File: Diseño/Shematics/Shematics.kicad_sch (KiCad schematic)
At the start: 2 parts, among them U1 ESP32-WROOM-E

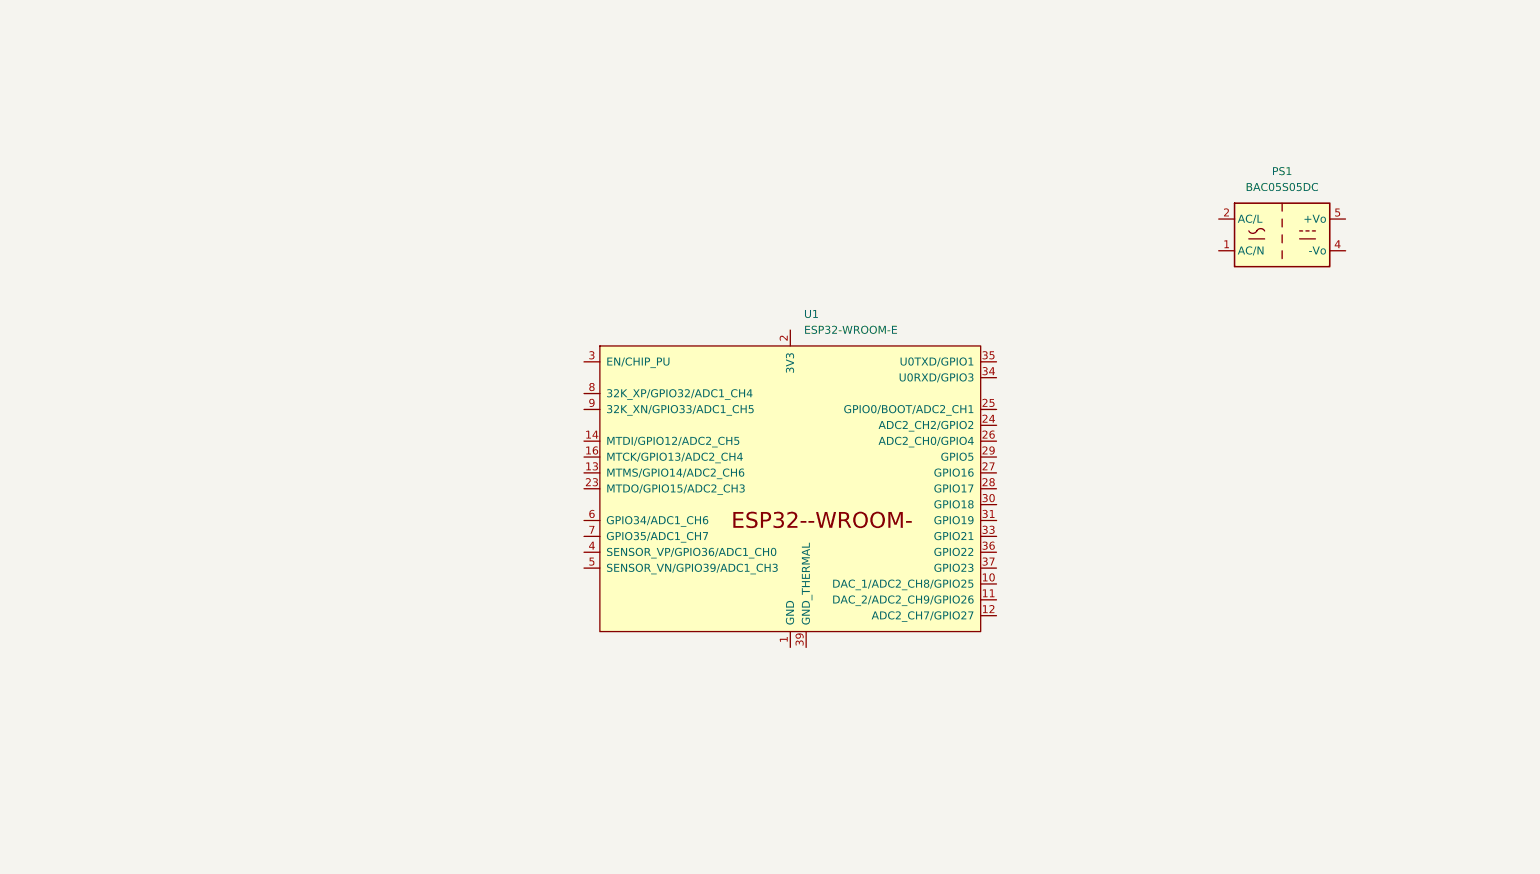
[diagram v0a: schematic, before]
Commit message: Cambios realizados sobre el documento de texto
Añadida tabla e índice de tablas y figuras junto con otros cambios
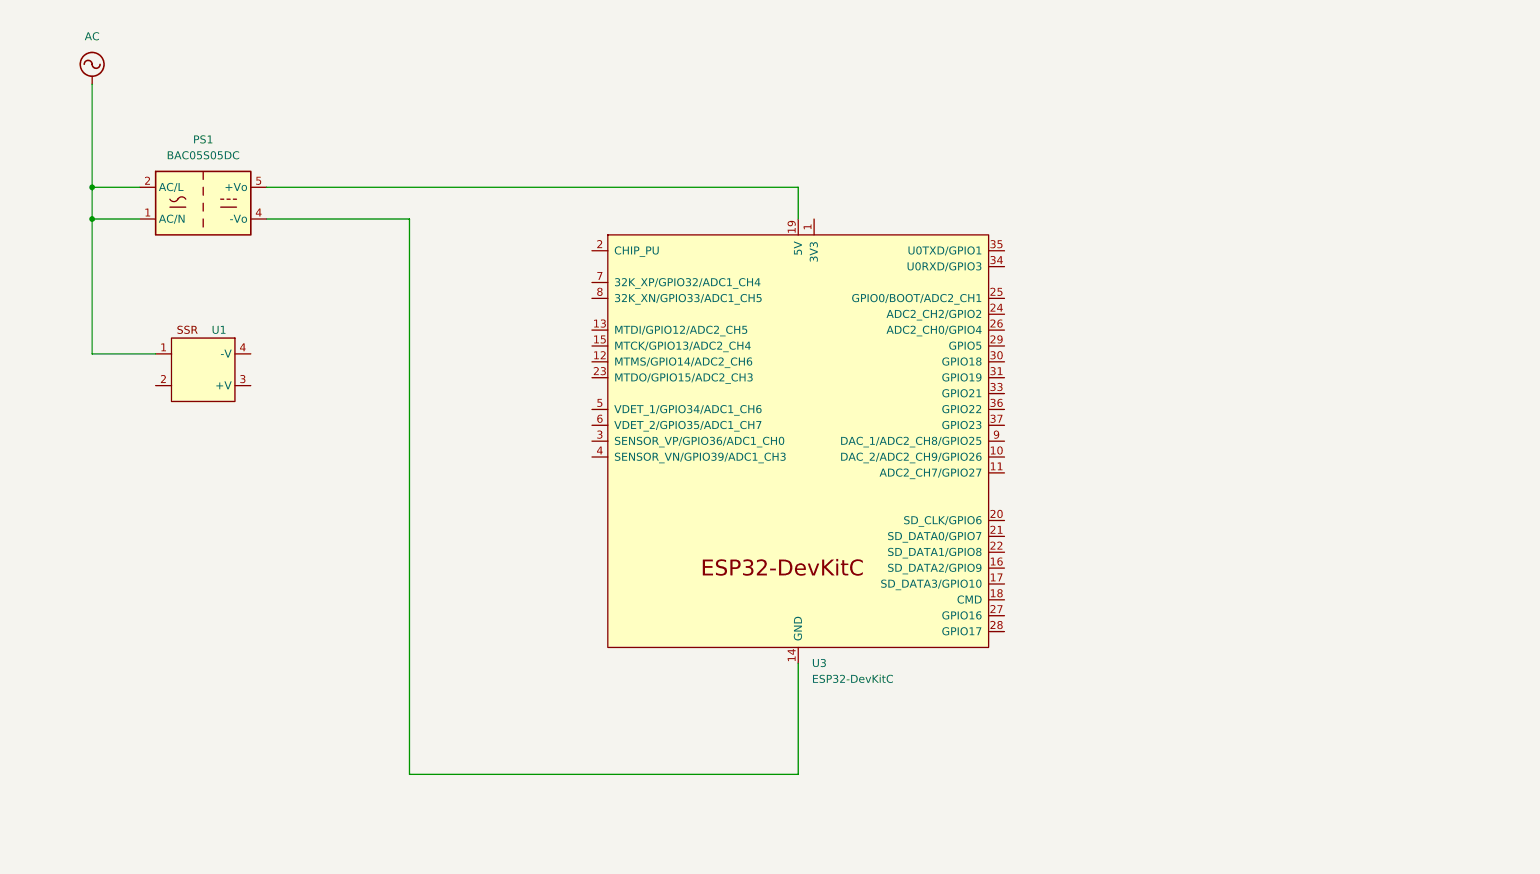
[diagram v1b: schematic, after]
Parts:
- removed U1: ESP32-WROOM-E, PCM_Espressif:ESP32-WROOM-32E, symbol PCM_Espressif:ESP32-WROOM-E
- added U1: ~, symbol Automating_the_care_of_a_plant:SSR
- added U3: ESP32-DevKitC, PCM_Espressif:ESP32-DevKitC, symbol PCM_Espressif:ESP32-DevKitC
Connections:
- net AC: now reaches PS1.1 (AC/N)
- net AC: now also PS1.2 (AC/L), U1.1
- net at PS1.4 (-Vo): now also U3.14 (GND), U3.32 (GND), U3.38 (GND)
- net at PS1.5 (+Vo): now also U3.19 (5V)
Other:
- moved on the sheet: PS1
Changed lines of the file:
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@@
     (company "Samuel Matamoros")
   )
-  (symbol (lib_id "Converter_ACDC:BAC05S05DC") (at 227.33 60.96 0) (unit 1)
+  (junction (at 36.83 53.34) (diameter 0) (color 0 0 0 0)
+  )
+  (junction (at 36.83 58.42) (diameter 0) (color 0 0 0 0)
+  )
+  (wire (pts (xy 44.45 58.42) (xy 36.83 58.42))
+    (stroke (width 0) (type default))
+  )
+  (wire (pts (xy 36.83 53.34) (xy 44.45 53.34))
+    (stroke (width 0) (type default))
+  )
+  (wire (pts (xy 149.86 53.34) (xy 149.86 58.42))
+    (stroke (width 0) (type default))
+  )
+  (wire (pts (xy 87.63 58.42) (xy 87.63 147.32))
+    (stroke (width 0) (type default))
+  )
+  (wire (pts (xy 36.83 80.01) (xy 46.99 80.01))
+    (stroke (width 0) (type default))
+  )
+  (wire (pts (xy 36.83 36.83) (xy 36.83 53.34))
+    (stroke (width 0) (type default))
+  )
+  (wire (pts (xy 87.63 147.32) (xy 149.86 147.32))
+    (stroke (width 0) (type default))
+  )
+  (wire (pts (xy 64.77 53.34) (xy 149.86 53.34))
+    (stroke (width 0) (type default))
+  )
+  (wire (pts (xy 64.77 58.42) (xy 87.63 58.42))
+    (stroke (width 0) (type default))
+  )
+  (wire (pts (xy 36.83 58.42) (xy 36.83 53.34))
+    (stroke (width 0) (type default))
+  )
+  (wire (pts (xy 149.86 147.32) (xy 149.86 129.54))
+    (stroke (width 0) (type default))
+  )
+  (wire (pts (xy 36.83 58.42) (xy 36.83 80.01))
+    (stroke (width 0) (type default))
+  )
+  (symbol (lib_id "Converter_ACDC:BAC05S05DC") (at 54.61 55.88 0) (unit 1)
     (in_bom yes) (on_board yes) (dnp no) (fields_autoplaced)
-    (property "Reference" "PS1" (at 227.33 50.8 0)
+    (property "Reference" "PS1" (at 54.61 45.72 0)
       (effects (font (size 1.27 1.27)))
     )
-    (property "Value" "BAC05S05DC" (at 227.33 53.34 0)
+    (property "Value" "BAC05S05DC" (at 54.61 48.26 0)
       (effects (font (size 1.27 1.27)))
     )
-    (property "Footprint" "Converter_ACDC:Converter_ACDC_Murata_BAC05SxxDC_THT" (at 227.33 69.85 0)
+    (property "Footprint" "Converter_ACDC:Converter_ACDC_Murata_BAC05SxxDC_THT" (at 54.61 64.77 0)
       (effects (font (size 1.27 1.27)) hide)
     )
-    (property "Datasheet" "https://www.murata.com/products/productdata/8809982558238/KAC-BAC05.pdf" (at 227.33 72.39 0)
+    (property "Datasheet" "https://www.murata.com/products/productdata/8809982558238/KAC-BAC05.pdf" (at 54.61 67.31 0)
       (effects (font (size 1.27 1.27)) hide)
     )
@@
     )
   )
-  (symbol (lib_id "PCM_Espressif:ESP32-WROOM-E") (at 148.59 101.6 0) (unit 1)
+  (symbol (lib_id "PCM_Espressif:ESP32-DevKitC") (at 149.86 93.98 0) (unit 1)
     (in_bom yes) (on_board yes) (dnp no) (fields_autoplaced)
-    (property "Reference" "U1" (at 150.7841 73.66 0)
+    (property "Reference" "U3" (at 152.0541 129.54 0)
       (effects (font (size 1.27 1.27)) (justify left))
     )
-    (property "Value" "ESP32-WROOM-E" (at 150.7841 76.2 0)
+    (property "Value" "ESP32-DevKitC" (at 152.0541 132.08 0)
       (effects (font (size 1.27 1.27)) (justify left))
     )
-    (property "Footprint" "PCM_Espressif:ESP32-WROOM-32E" (at 148.59 137.16 0)
+    (property "Footprint" "PCM_Espressif:ESP32-DevKitC" (at 149.86 137.16 0)
       (effects (font (size 1.27 1.27)) hide)
     )
-    (property "Datasheet" "https://www.espressif.com/sites/default/files/documentation/esp32-wroom-32e_esp32-wroom-32ue_datasheet_en.pdf" (at 148.59 139.7 0)
+    (property "Datasheet" "https://docs.espressif.com/projects/esp-idf/zh_CN/latest/esp32/hw-reference/esp32/get-started-devkitc.html" (at 149.86 139.7 0)
       (effects (font (size 1.27 1.27)) hide)
     )
+    (pin "9")
+    (pin "38")
+    (pin "10")
+    (pin "22")
+    (pin "11")
+    (pin "1")
+    (pin "15")
+    (pin "20")
+    (pin "13")
+    (pin "5")
+    (pin "30")
+    (pin "21")
+    (pin "23")
+    (pin "18")
+    (pin "33")
+    (pin "37")
+    (pin "16")
+    (pin "17")
     (pin "12")
+    (pin "26")
+    (pin "6")
+    (pin "34")
+    (pin "32")
+    (pin "36")
+    (pin "28")
+    (pin "3")
+    (pin "14")
+    (pin "8")
+    (pin "27")
+    (pin "35")
+    (pin "4")
+    (pin "31")
+    (pin "24")
+    (pin "7")
+    (pin "2")
+    (pin "29")
+    (pin "19")
+    (pin "25")
+    (instances
+      (project "Shematics"
+        (path "/635a2275-8ba1-4139-998c-8b290d348422"
+          (reference "U3") (unit 1)
+        )
+      )
+    )
+  )
+  (symbol (lib_id "Automating_the_care_of_a_plant:SSR") (at 54.61 82.55 0) (mirror y) (unit 1)
+    (in_bom yes) (on_board yes) (dnp no)
+    (property "Reference" "U1" (at 57.15 76.2 0)
+      (effects (font (size 1.27 1.27)))
+    )
+    (property "Value" "~" (at 50.8 82.55 0)
+      (effects (font (size 1.27 1.27)))
+    )
+    (property "Footprint" "" (at 55.88 83.82 0)
+      (effects (font (size 1.27 1.27)) hide)
+    )
+    (property "Datasheet" "" (at 55.88 83.82 0)
+      (effects (font (size 1.27 1.27)) hide)
+    )
+    (pin "3")
+    (pin "2")
     (pin "1")
-    (pin "29")
-    (pin "8")
-    (pin "26")
-    (pin "3")
-    (pin "34")
-    (pin "35")
-    (pin "6")
-    (pin "23")
-    (pin "13")
-    (pin "36")
-    (pin "2")
-    (pin "16")
-    (pin "25")
-    (pin "38")
-    (pin "27")
-    (pin "39")
-    (pin "10")
-    (pin "31")
-    (pin "9")
-    (pin "33")
     (pin "4")
-    (pin "7")
-    (pin "37")
-    (pin "24")
-    (pin "5")
-    (pin "15")
-    (pin "28")
-    (pin "11")
-    (pin "14")
-    (pin "30")
     (instances
       (project "Shematics"
@@
         )
       )
+    )
+  )
+  (symbol (lib_id "power:AC") (at 36.83 36.83 0) (unit 1)
+    (in_bom yes) (on_board yes) (dnp no) (fields_autoplaced)
+    (property "Reference" "#PWR01" (at 36.83 39.37 0)
+      (effects (font (size 1.27 1.27)) hide)
+    )
+    (property "Value" "AC" (at 36.83 29.21 0)
+      (effects (font (size 1.27 1.27)))
+    )
+    (property "Footprint" "" (at 36.83 36.83 0)
+      (effects (font (size 1.27 1.27)) hide)
+    )
+    (property "Datasheet" "" (at 36.83 36.83 0)
+      (effects (font (size 1.27 1.27)) hide)
+    )
+    (pin "1")
+    (instances
+      (project "Shematics"
+        (path "/635a2275-8ba1-4139-998c-8b290d348422"
+          (reference "#PWR01") (unit 1)
+        )
+      )

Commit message: Modificado el esquema electrónico y el documento
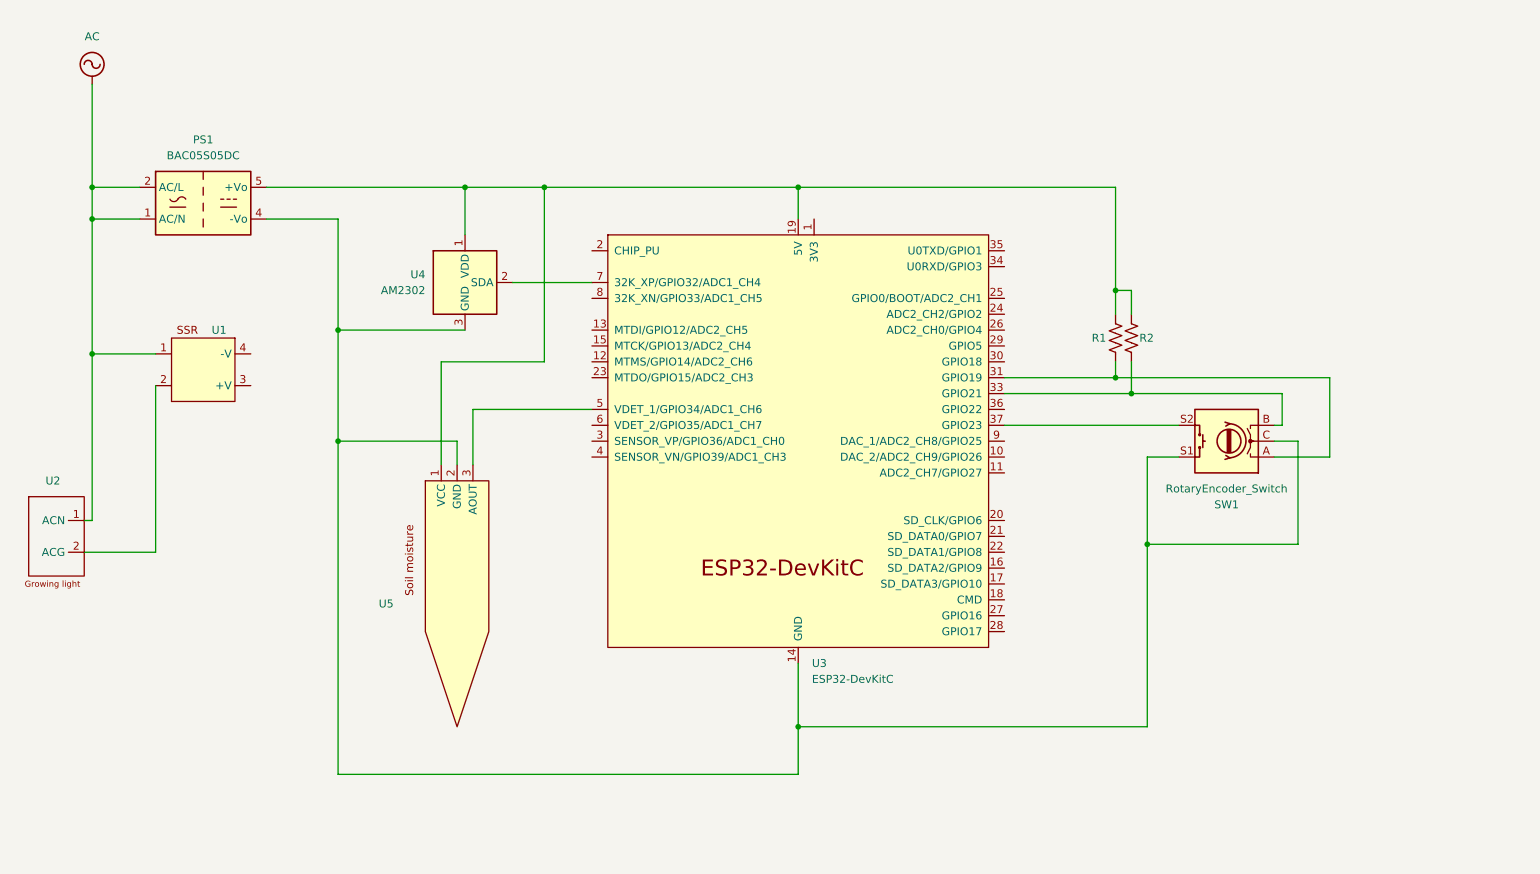
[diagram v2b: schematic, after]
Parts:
- added R1, R2: R_US, symbol Device:R_US
- added SW1: RotaryEncoder_Switch, symbol Device:RotaryEncoder_Switch
- added U2: ~, symbol Automating_the_care_of_a_plant:Growing_light
- added U4: AM2302, Sensor:ASAIR_AM2302_P2.54mm_Vertical, symbol Sensor:AM2302
- added U5: ~, symbol Automating_the_care_of_a_plant:Soil_Moisture
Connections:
- net AC: now also U2.1 (ACN)
- net at PS1.4 (-Vo), U3.14 (GND), U3.32 (GND)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: now also SW1.C, SW1.S1, U4.3 (GND), U4.4 (GND), U5.2 (GND)
- net at PS1.5 (+Vo), U3.19 (5V): now also R1.1, R2.1, U4.1 (VDD), U5.1 (VCC)
- net at U3.31 (GPIO19): now also R1.2, SW1.A
- net at U3.33 (GPIO21): now also R2.2, SW1.B
- net at U3.37 (GPIO23): now also SW1.S2
- net at U3.5 (VDET_1/GPIO34/ADC1_CH6): now also U5.3 (AOUT)
- net at U3.7 (32K_XP/GPIO32/ADC1_CH4): now also U4.2 (SDA)
- net at U1.2: now also U2.2 (ACG)

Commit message: Terminado el esquema electrónico y añadido un pequeño test con el fotoresistor
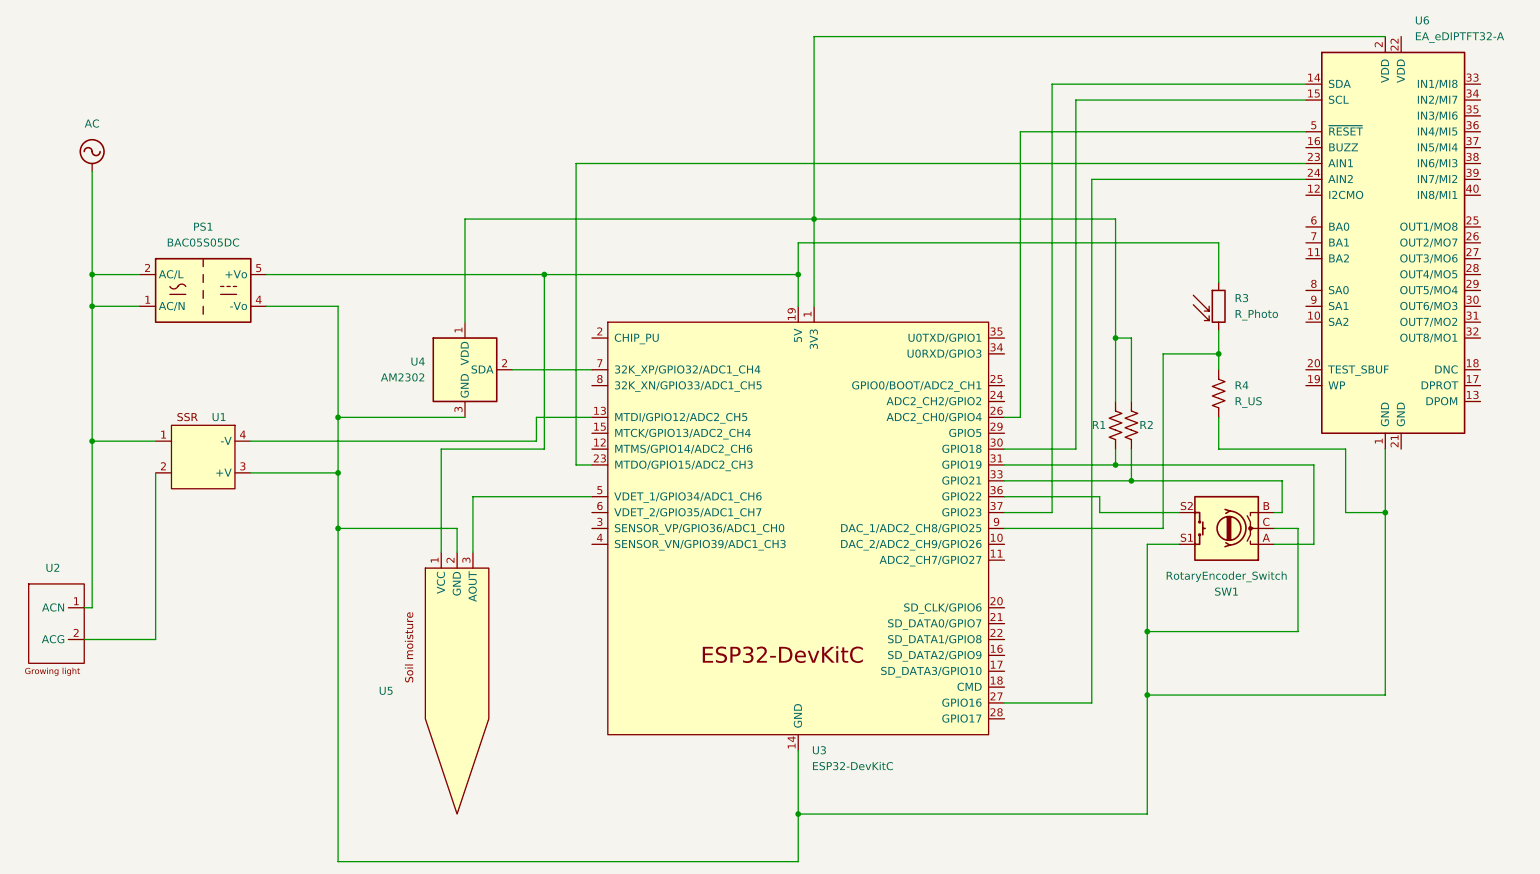
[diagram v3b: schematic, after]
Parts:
- added R3: R_Photo, symbol Device:R_Photo
- added R4: R_US, symbol Device:R_US
- added U6: EA_eDIPTFT32-A, Display:EA_eDIPTFT32-XXX, symbol Display_Graphic:EA_eDIPTFT32-A
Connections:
- net at PS1.4 (-Vo), SW1.C, SW1.S1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: now also U1.3 (+V), R4.2, U6.1 (GND)
- net at PS1.5 (+Vo), U3.19 (5V), U5.1 (VCC): now also R3.1; no longer R1.1, R2.1, U4.1 (VDD)
- net at U3.1 (3V3): now also R1.1, R2.1, U4.1 (VDD), U6.2 (VDD)
- net at U3.13 (MTDI/GPIO12/ADC2_CH5): now also U1.4 (-V)
- net at U3.23 (MTDO/GPIO15/ADC2_CH3): now also U6.23 (AIN1)
- net at U3.26 (ADC2_CH0/GPIO4): now also U6.5 (~{RESET})
- net at U3.27 (GPIO16): now also U6.24 (AIN2)
- net at U3.30 (GPIO18): now also U6.15 (SCL)
- net at U3.36 (GPIO22): now also SW1.S2
- net at U3.37 (GPIO23): now also U6.14 (SDA); no longer SW1.S2
- net at U3.9 (DAC_1/ADC2_CH8/GPIO25): now also R3.2, R4.1
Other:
- moved on the sheet: PS1, R1, R2, SW1, U1, U2, U3, U4, U5

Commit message: Modificado el documento, queda por rehacer la estructura y anexar el código
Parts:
- added U7: ~, symbol Automating_the_care_of_a_plant:WaterPump
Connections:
- net at PS1.4 (-Vo), R4.2, SW1.C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: now also U7.2 (-)
- net at U3.11 (ADC2_CH7/GPIO27): now also U7.1 (+)
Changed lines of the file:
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@@
   (junction (at 149.86 67.31) (diameter 0) (color 0 0 0 0)
   )
+  (junction (at 205.74 153.67) (diameter 0) (color 0 0 0 0)
+  )
   (junction (at 205.74 124.46) (diameter 0) (color 0 0 0 0)
   )
@@
     (stroke (width 0) (type default))
   )
+  (wire (pts (xy 191.77 113.03) (xy 191.77 148.59))
+    (stroke (width 0) (type default))
+  )
   (wire (pts (xy 96.52 74.93) (xy 96.52 58.42))
     (stroke (width 0) (type default))
@@
     (stroke (width 0) (type default))
   )
+  (wire (pts (xy 220.98 153.67) (xy 205.74 153.67))
+    (stroke (width 0) (type default))
+  )
   (wire (pts (xy 76.2 107.95) (xy 76.2 161.29))
     (stroke (width 0) (type default))
   )
+  (wire (pts (xy 182.88 113.03) (xy 191.77 113.03))
+    (stroke (width 0) (type default))
+  )
   (wire (pts (xy 35.56 120.65) (xy 36.83 120.65))
     (stroke (width 0) (type default))
@@
   )
   (wire (pts (xy 76.2 72.39) (xy 76.2 90.17))
+    (stroke (width 0) (type default))
+  )
+  (wire (pts (xy 191.77 148.59) (xy 220.98 148.59))
     (stroke (width 0) (type default))
   )
@@
         )
       )
+    )
+  )
+  (symbol (lib_id "Automating_the_care_of_a_plant:WaterPump") (at 229.87 151.13 0) (unit 1)
+    (in_bom yes) (on_board yes) (dnp no) (fields_autoplaced)
+    (property "Reference" "U7" (at 238.76 149.3492 0)
+      (effects (font (size 1.27 1.27)) (justify left))
+    )
+    (property "Value" "~" (at 227.33 148.59 0)
+      (effects (font (size 1.27 1.27)))
+    )
+    (property "Footprint" "" (at 227.33 148.59 0)
+      (effects (font (size 1.27 1.27)) hide)
+    )
+    (property "Datasheet" "" (at 227.33 148.59 0)
+      (effects (font (size 1.27 1.27)) hide)
+    )
+    (pin "2")
+    (pin "1")
+    (instances
+      (project "Shematics"
+        (path "/635a2275-8ba1-4139-998c-8b290d348422"
+          (reference "U7") (unit 1)
+        )
+      )
